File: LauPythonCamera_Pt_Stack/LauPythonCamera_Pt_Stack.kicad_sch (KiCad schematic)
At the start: 17 parts, among them U1 NOIP1SN1300A-QDI

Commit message: hw(camera): fix pin plan — all 7 LVDS pairs must be on the DF40's odd row
The previous pin plan was wrong and would have cost a board spin.

The DF40's two rows escape in OPPOSITE directions. Measured from the footprint
already used on LauMipiCamera/LauCameraTrigger (DF40C-80DP-0.4V): odd pins sit
at y=+1.355mm, even pins at y=-1.355mm. The old plan put sync/dout0/dout2 on
even-row pairs (B40/42, B46/48, B52/54) — those three would have escaped out the
FAR side of the connector, away from the sensor, forcing each to loop around the
connector body or via down to another layer. The .kicad_dru flags exactly that as
a warning.

Alchitry's pairs are always (odd, odd+2) or (even, even+2), so both halves of a
pair are always in the same row. Bank 13 has exactly 8 odd-row and 8 even-row
pairs; we need 7. Both MRCC pairs — (B39,B41) and (B45,B47) — are odd-row. So all
seven fit on the odd row AND the forwarded bit clock still lands on an MRCC.

Ordering also fixed. All six sensor LVDS outputs occupy one contiguous edge of
the LCC (pins 7-18, no power interleaved), and lvds_clock_in (23/24) sits just
around the corner. Assigning connector pairs in that same sequence means nothing
crosses, and since N is the lower pin number on BOTH the sensor and the
connector, P/N aligns with no intra-pair swap. Orient U1 with pin 7 toward B39.

Result: seven straight, parallel, via-free pairs on F.Cu over solid ground.

Also in this commit:

- 4-LAYER STACKUP. Both existing stacked boards are 2-layer, which cannot hold a
  controlled 100R at 720 Mbps — the only reference plane is 1.6mm away across the
  core. (Tell: LauMipiCamera's .kicad_dru describes "~0.1mm prepreg to the GND
  plane" — a 4-layer description in a 2-layer board, with width/gap left as
  explicit placeholders. That impedance was never resolved.) This board targets
  JLCPCB JLC04161H-7628: LVDS on F.Cu over solid GND on In1.Cu, 0.2104mm of 7628
  prepreg between. W=0.24mm / S=0.20mm -> ~100R (IPC-2141 approx; confirm with
 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
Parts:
- C1, C10, C11, C2, C3, C4, C5, C6, C7, C8, C9: footprint (none) -> Capacitor_SMD:C_0402_1005Metric
- C12, C13, C14: footprint (none) -> Capacitor_SMD:C_0805_2012Metric
- R1, R2: footprint (none) -> Resistor_SMD:R_0402_1005Metric

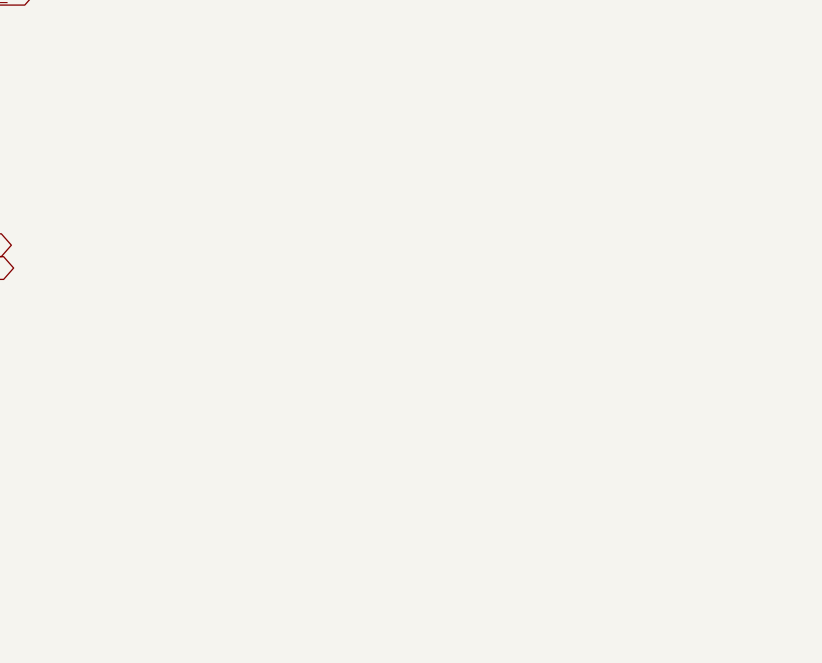
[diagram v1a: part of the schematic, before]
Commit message: hw(camera): power-on-safe pulls + complete the XDC pin map
Two related fixes, both from the same root cause: FPGA user I/O are Hi-Z until
DONE goes high, so between power-up and bitstream load every control line into
the sensor floats.

1. POWER-ON-SAFE PULLS (R3-R7, 10k 0402). The schematic had none.

     ss_n     PULL-UP    a floating SPI select could read as ASSERTED, and the
                         sensor would clock in garbage from a floating sck/mosi
     reset_n  PULL-DOWN  holds the sensor in reset until the FPGA is configured
                         and deliberately releases it (fail-safe direction)
     trigger0-2 PULL-DOWN   no spurious exposures during configuration

   The XDC also sets BITSTREAM.CONFIG.UNUSEDPIN PULLDOWN so the FPGA's weak
   internal pulls agree with the external ones rather than fight them. The
   external resistors are the primary guarantee: the bitstream setting does
   nothing before the bitstream loads, which is exactly the window that matters.

   Note we do NOT need I2C pull-ups. Unlike LauMipiCamera (R_SCL/R_SDA at 4k7),
   the PYTHON talks SPI, not I2C.

2. BANK 14 / BANK 35 SPLIT, and the control pins are now filled in.

   A3-A6 are bank 14 = the Artix-7 CONFIGURATION bank. A9-A18 are bank 35 =
   ordinary IO. Everything that could disturb the sensor while floating is now
   on bank 35 with an external pull; bank 14 carries only signals that are
   harmless floating (mosi, sck — inert while ss_n is deasserted — miso, and
   clk_pll, which is unused entirely since the PLL is bypassed).

   Confirmed from PtV2TopPin.kt that banks 14/35 are HARDWIRED 3.3 V:
   bankToVcco() returns a single-element ["3.3"] for banks 14/16/34/35 and only
   bank 13 returns ["3.3","2.5","1.8"]. VBSEL strapping controls bank 13 and
   nothing else, so the 3.3 V control bank and the 2.5 V LVDS bank are
   electrically independent. Package pins cross-checked against the Xilinx
   xc7a100tfgg484pkg.csv, as with bank 13.

pt_camera.xdc is now compl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
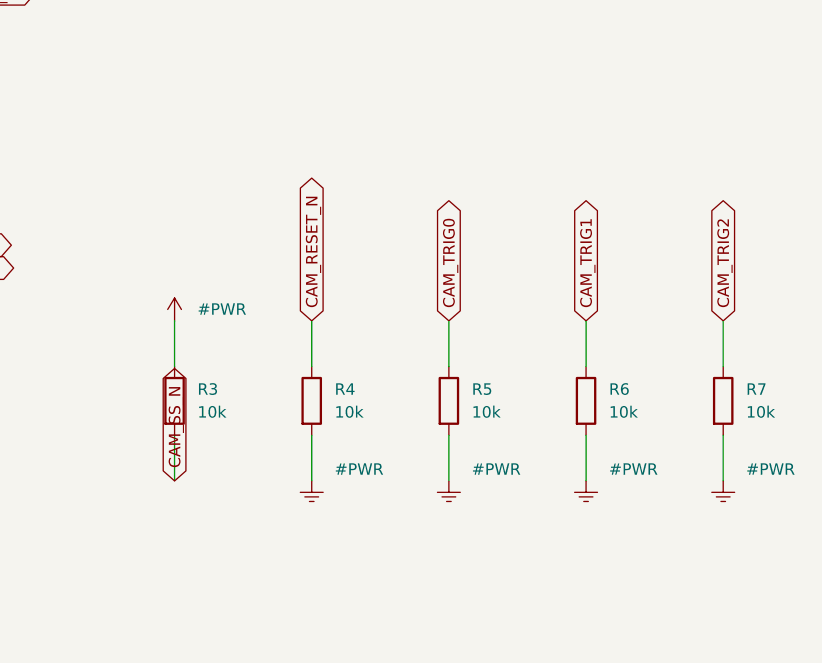
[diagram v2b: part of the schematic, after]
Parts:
- added R3, R4, R5, R6, R7: 10k, Resistor_SMD:R_0402_1005Metric, symbol Device:R
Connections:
- net +3V3_CAM: now also R3.1
- net CAM_RESET_N: now also R4.1
- net CAM_SS_N: now also R3.2
- net CAM_TRIG0: now also R5.1
- net CAM_TRIG1: now also R6.1
- net CAM_TRIG2: now also R7.1
- net GND: now also R4.2, R5.2, R6.2, R7.2

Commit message: hw(camera): DF40 connectors + regulator chain — schematic complete
Adds J1/J2/J3 and the three sensor rails. Every net verified: 31 nets, zero
mismatches, no orphans, 102 no-connects on unused connector pins.

CONNECTORS
  J1  DF40C-80DP  Bank A   11 single-ended control signals (banks 14/35, 3.3V)
  J2  DF40C-80DP  Bank B   the 7 LVDS pairs (bank 13, 2.5V), ALL on the ODD row
  J3  DF40C-50DP  Control  all element power + the VBSEL straps

The 80-pin symbol puts ODD pins on the left and EVEN on the right, mirroring the
connector's two physical rows (verified from the footprint: odd at y=+1.355,
even at y=-1.355). Each differential pair (odd, odd+2) therefore lands adjacent
on the same side of the symbol, and the row split that drives the whole layout is
visible in the schematic instead of buried in a table.

J1 and J2 carry NO power pins — only IO and GND. Every volt arrives on J3.

REGULATORS — three decisions that each look odd in isolation:

1. vdd_pix gets its OWN +/-1% LDO fed from VDD, not from the 3.3V rail. The sensor
   demands 3.25-3.35V. A +/-2% tolerance on a nominal 3.3V rail is 3.23-3.37V —
   ALREADY OUTSIDE that window — and you cannot LDO 3.3V down to 3.3V. So it has
   to come from VDD. Current is ~5mA, so even at VDD=12V that is <90mW: no thermal
   problem. U4 MUST be specified +/-1% or better; a garden-variety +/-2% 3.3V LDO
   does not meet the window. This is the one part where the datasheet's tolerance
   line actually bites.

2. vdd_33 gets a LOAD SWITCH, not a regulator. It is already 3.3V so nothing needs
   regulating — but it needs an ENABLE, because a straight rail tap comes up
   whenever the board does, which violates the power-up order. The switch exists
   purely so vdd_33 can be sequenced.

3. Sequencing is an RC cascade (R8-R10, C15-C17); each stage's output enables the
   next, giving vdd_18 -> vdd_33 -> vdd_pix — the datasheet order — with ~1ms
   between stages, comfortably over the 10us minimum. Power-DOWN is not sequenced;
 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
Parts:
- added C15, C16, C17: 100n, Capacitor_SMD:C_0402_1005Metric, symbol Device:C
- added C18, C19: 10u, Capacitor_SMD:C_0805_2012Metric, symbol Device:C
- added J1: DF40C-80DP (Bank A), Connector_Hirose_DF40:Hirose_DF40C-80DP-0.4V_2x40-1MP_P0.4mm, symbol LauSensors:DF40C-80DP
- added J2: DF40C-80DP (Bank B), Connector_Hirose_DF40:Hirose_DF40C-80DP-0.4V_2x40-1MP_P0.4mm, symbol LauSensors:DF40C-80DP
- added J3: DF40C-50DP (Control), Connector_Hirose_DF40:Hirose_DF40C-50DP-0.4V_2x25-1MP_P0.4mm, symbol LauSensors:DF40C-50DP
- added R10, R8, R9: 10k, Resistor_SMD:R_0402_1005Metric, symbol Device:R
- added R11, R12: 1k, Resistor_SMD:R_0402_1005Metric, symbol Device:R
- added U2: AP2112K-1.8 LDO, Package_TO_SOT_SMD:SOT-23-5, symbol LauSensors:REG_5PIN_EN
- added U3: Load switch 3V3, Package_TO_SOT_SMD:SOT-23-5, symbol LauSensors:REG_5PIN_EN
- added U4: LDO 3V3 1pct vdd_pix, Package_TO_SOT_SMD:SOT-23-5, symbol LauSensors:REG_5PIN_EN
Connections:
- net +1V8_CAM: now also R9.1, U2.5 (VOUT)
- net +3V3_CAM: now also R10.1, U3.5 (VOUT)
- net +3V3_PIX: now also U4.5 (VOUT)
- net CAM_CLKOUT_N: now also J2.39 (P39)
- net CAM_CLKOUT_P: now also J2.41 (P41)
- net CAM_CLK_PLL: now also J1.6 (P6)
- net CAM_D0_N: now also J2.45 (P45)
- net CAM_D0_P: now also J2.47 (P47)
- net CAM_D1_N: now also J2.51 (P51)
- net CAM_D1_P: now also J2.53 (P53)
- net CAM_D2_N: now also J2.57 (P57)
- net CAM_D2_P: now also J2.59 (P59)
- net CAM_D3_N: now also J2.63 (P63)
- net CAM_D3_P: now also J2.65 (P65)
- net CAM_LVDSCLK_N: now also J2.75 (P75)
- net CAM_LVDSCLK_P: now also J2.77 (P77)
- net CAM_MISO: now also J1.4 (P4)
- net CAM_MON0: now also J1.16 (P16)
- net CAM_MON1: now also J1.17 (P17)
- net CAM_MOSI: now also J1.3 (P3)
- net CAM_RESET_N: now also J1.9 (P9)
- net CAM_SCK: now also J1.5 (P5)
- net CAM_SS_N: now also J1.10 (P10)
- net CAM_SYNC_N: now also J2.69 (P69)
- net CAM_SYNC_P: now also J2.71 (P71)
- net CAM_TRIG0: now also J1.11 (P11)
- net CAM_TRIG1: now also J1.12 (P12)
- net CAM_TRIG2: now also J1.15 (P15)
- net GND: now also C15.2, C16.2, C17.2, C18.2, C19.2, J1.1 (P1), J1.13 (P13), J1.14 (P14), J1.19 (P19), J1.2 (P2), J1.20 (P20), J1.25 (P25), J1.26 (P26), J1.31 (P31), J1.32 (P32), J1.37 (P37), J1.38 (P38), J1.43 (P43), J1.44 (P44), J1.49 (P49), J1.50 (P50), J1.55 (P55), J1.56 (P56), J1.61 (P61), J1.62 (P62), J1.67 (P67), J1.68 (P68), J1.7 (P7), J1.73 (P73), J1.74 (P74), J1.79 (P79), J1.8 (P8), J1.80 (P80), J2.1 (P1), J2.13 (P13), J2.14 (P14), J2.19 (P19), J2.2 (P2), J2.20 (P20), J2.25 (P25), J2.26 (P26), J2.31 (P31), J2.32 (P32), J2.37 (P37), J2.38 (P38), J2.43 (P43), J2.44 (P44), J2.49 (P49), J2.50 (P50), J2.55 (P55), J2.56 (P56), J2.61 (P61), J2.62 (P62), J2.67 (P67), J2.68 (P68), J2.7 (P7), J2.73 (P73), J2.74 (P74), J2.79 (P79), J2.8 (P8), J2.80 (P80), J3.17 (C17), J3.18 (C18), J3.19 (C19), J3.20 (C20), J3.21 (C21), J3.22 (C22), J3.23 (C23), J3.24 (C24), J3.25 (C25), J3.26 (C26), J3.27 (C27), J3.28 (C28), U2.2 (GND), U3.2 (GND), U4.2 (GND)
- new net +3V3_SYS: C18.1, J3.1 (C1), J3.11 (C11), J3.13 (C13), J3.15 (C15), J3.3 (C3), J3.5 (C5), J3.7 (C7), J3.9 (C9), R11.1, R12.1, R8.1, U2.1 (VIN), U3.1 (VIN)
- new net SEQ_1V8: C15.1, R8.2, U2.3 (EN)
- new net SEQ_3V3: C16.1, R9.2, U3.3 (EN)
- new net SEQ_PIX: C17.1, R10.2, U4.3 (EN)
- new net VBSEL_A: J3.38 (C38), R11.2
- new net VBSEL_B: J3.40 (C40), R12.2
- new net VDD_SYS: C19.1, J3.10 (C10), J3.12 (C12), J3.14 (C14), J3.16 (C16), J3.2 (C2), J3.4 (C4), J3.6 (C6), J3.8 (C8), U4.1 (VIN)
- no-connect marks 0 -> 102

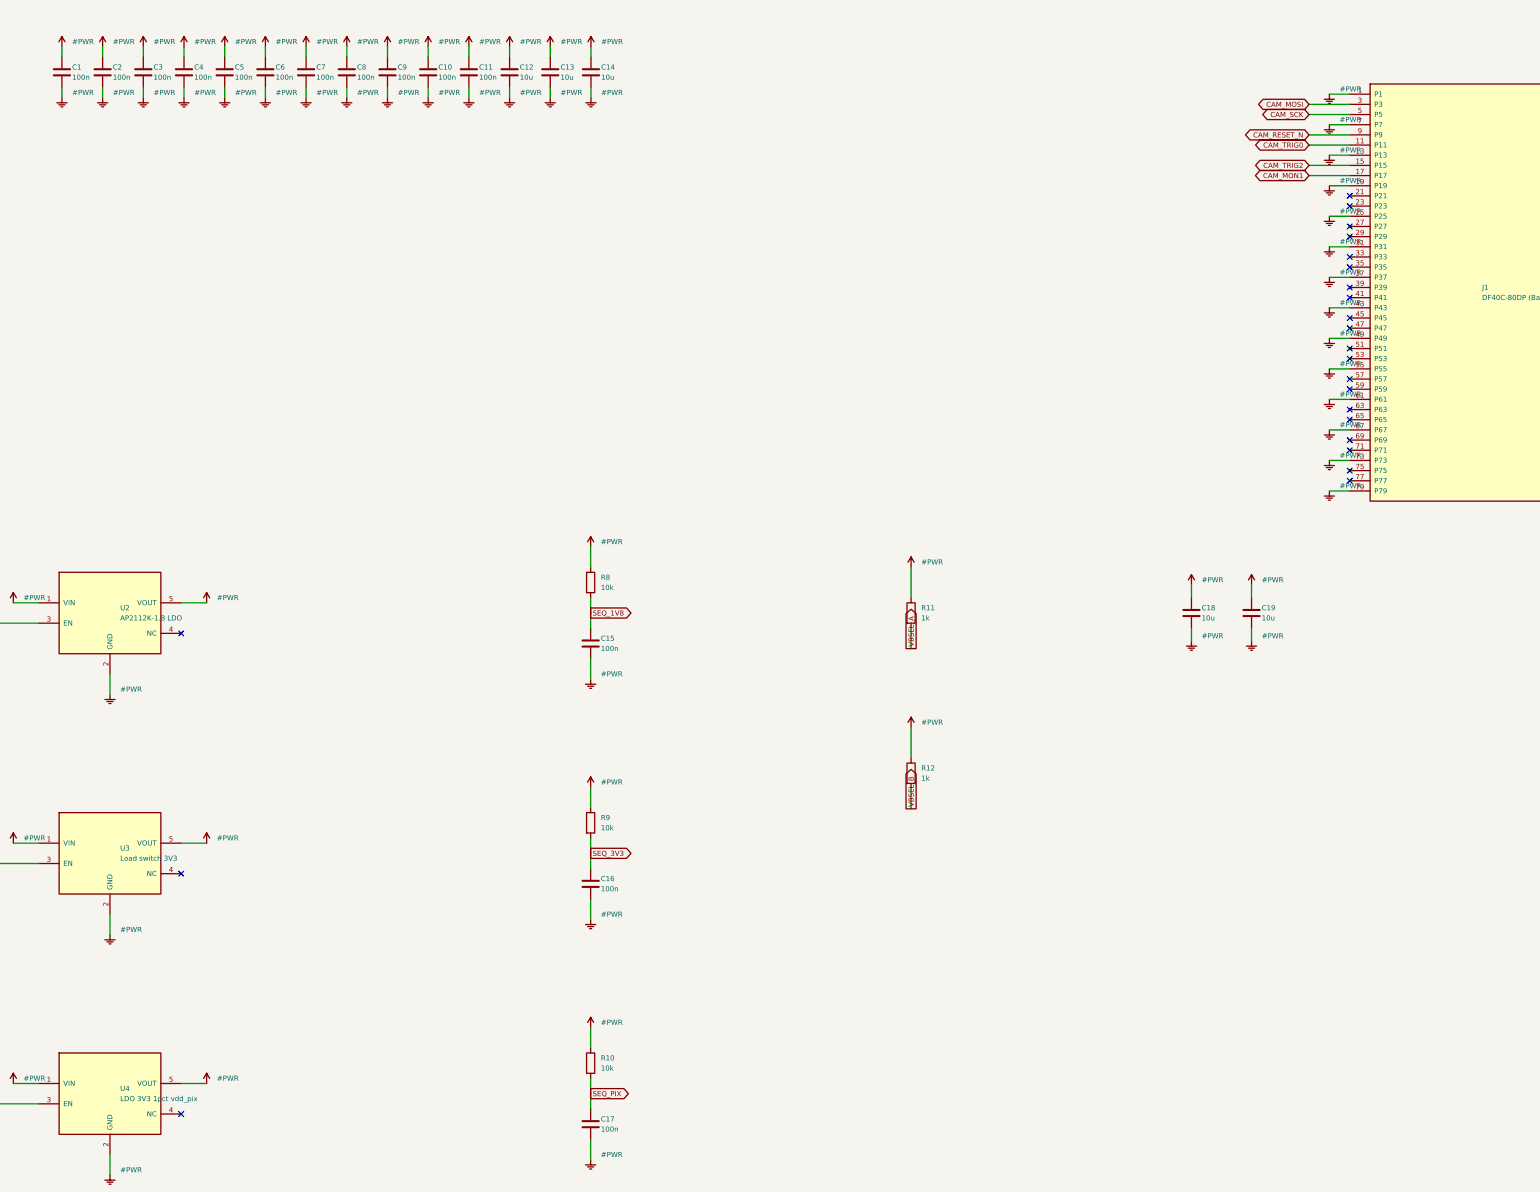
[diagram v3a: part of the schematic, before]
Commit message: hw(camera): apply three fixes learned from a fabbed board (ruffner/lupa300)
Compared this schematic against ruffner/lupa300 -> pcb/uZed/lupa-hdmi-carrier.sch,
a MANUFACTURED FPGA carrier for a LUPA300 in the SAME Andon LCC48 socket. Three
changes came out of it.

1. FB1 — FERRITE BEAD ON vdd_pix.  Their board beads VPIX, VDDA and VADC (BLM18).
   We had NOTHING on the pixel supply, which is the most noise-sensitive rail on
   the sensor. This was a genuine omission, not a simplification. U4 -> FB1 -> the
   sensor.

2. U4 -> ADP7158-3.3.  They used the ADP7158 (ultra-low-noise, high-PSRR, +/-0.8%)
   for their sensitive rails. It meets the vdd_pix 3.25-3.35V window with margin,
   where a garden-variety +/-2% 3.3V LDO does not. This replaces my vague
   "+/-1% or better" with a part that a working board actually used.

3. Per-pin decoupling 100n -> 1u (C1-C11), plus C20-C22 (100n per rail).  Their
   primary decoupler is 1uF, not 100nF, backed by 0.1uF. A modern 1uF X7R in 0402
   has similar ESL to a 100nF but 10x the capacitance, so it holds supply impedance
   down across a wider band.

TWO THINGS FROM THAT BOARD WE DELIBERATELY DID NOT COPY:

- Their bias network. Every LUPA300 bias pin has an R AND a C, and it is tempting
  to look at our bare R1 and think a cap is missing. It is not. Those are VOLTAGE
  nodes fed by RC dividers; the PYTHON's ibias_master is a CURRENT REFERENCE — the
  47k to gnd_33 sets a reference current and the datasheet specifies nothing else.
  Hanging a cap on a current-set node is not obviously safe and onsemi does not ask
  for one.

- Their LVDS termination — because they have none. The LUPA300 is a PARALLEL sensor
  (D0-D9, FRAME_VALID, LINE_VALID). Their board tells us nothing about our
  termination scheme; the 51R networks on it are not on the sensor.

They also clock their sensor from a local SI514 oscillator. We deliberately do the
opposite and drive the LVDS clock from the FPGA — a local oscillator would break
phase-lock to the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
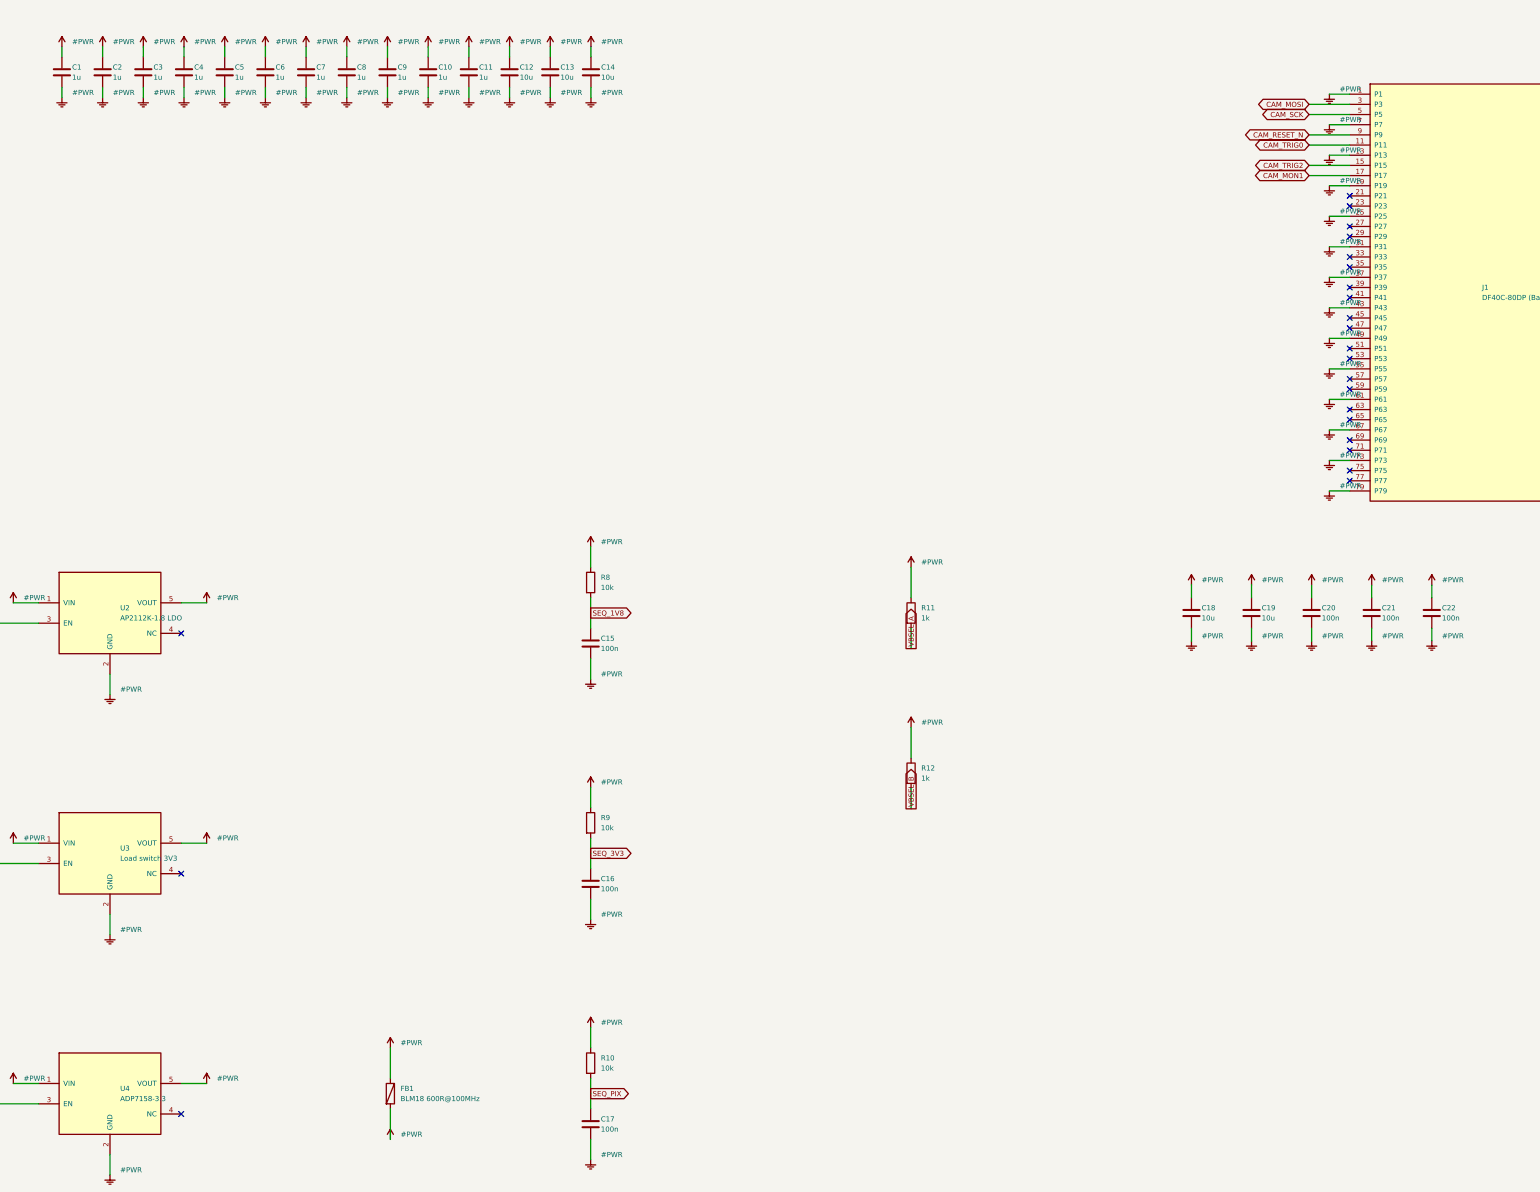
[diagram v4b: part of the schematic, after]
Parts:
- added C20, C21, C22: 100n, Capacitor_SMD:C_0402_1005Metric, symbol Device:C
- added FB1: BLM18 600R@100MHz, Inductor_SMD:L_0603_1608Metric, symbol Device:FerriteBead
- C1, C10, C11, C2, C3, C4, C5, C6, C7, C8, C9: value 100n -> 1u
- U4: value LDO 3V3 1pct vdd_pix -> ADP7158-3.3
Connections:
- net +1V8_CAM: now also C21.1
- net +3V3_CAM: now also C20.1
- net +3V3_PIX: now also C22.1, FB1.2; no longer U4.5 (VOUT)
- net GND: now also C20.2, C21.2, C22.2
- new net +3V3_PIX_RAW: FB1.1, U4.5 (VOUT)
